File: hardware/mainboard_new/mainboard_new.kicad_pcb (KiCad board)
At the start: 2 copper layers, 59.4 x 34.5 mm, 11 parts, among them M1 LOGIC_LEVEL_CONVERTER, Q1 BS170

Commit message: #9 More rework at the pcb
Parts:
- moved 5vPower1 8.66 mm to (136.9, 97.5), turned to 180 degrees
- moved MOTOR_DRV1 3.36 mm to (144.3, 85.3)
- moved Motor_OUT1 2.86 mm to (136.7, 85.9)
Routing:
- net +5V: track 55.0 -> 44.1 mm
- net Net-(MOTOR_DRV1-Pad3): track 5.78 -> 4.55 mm
- net +3V3: track 33.0 -> 31.8 mm
- net Net-(100K1-Pad1): track 52.9 -> 52.1 mm
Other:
- board size 59.4 x 34.5 mm -> 59.4 x 32 mm

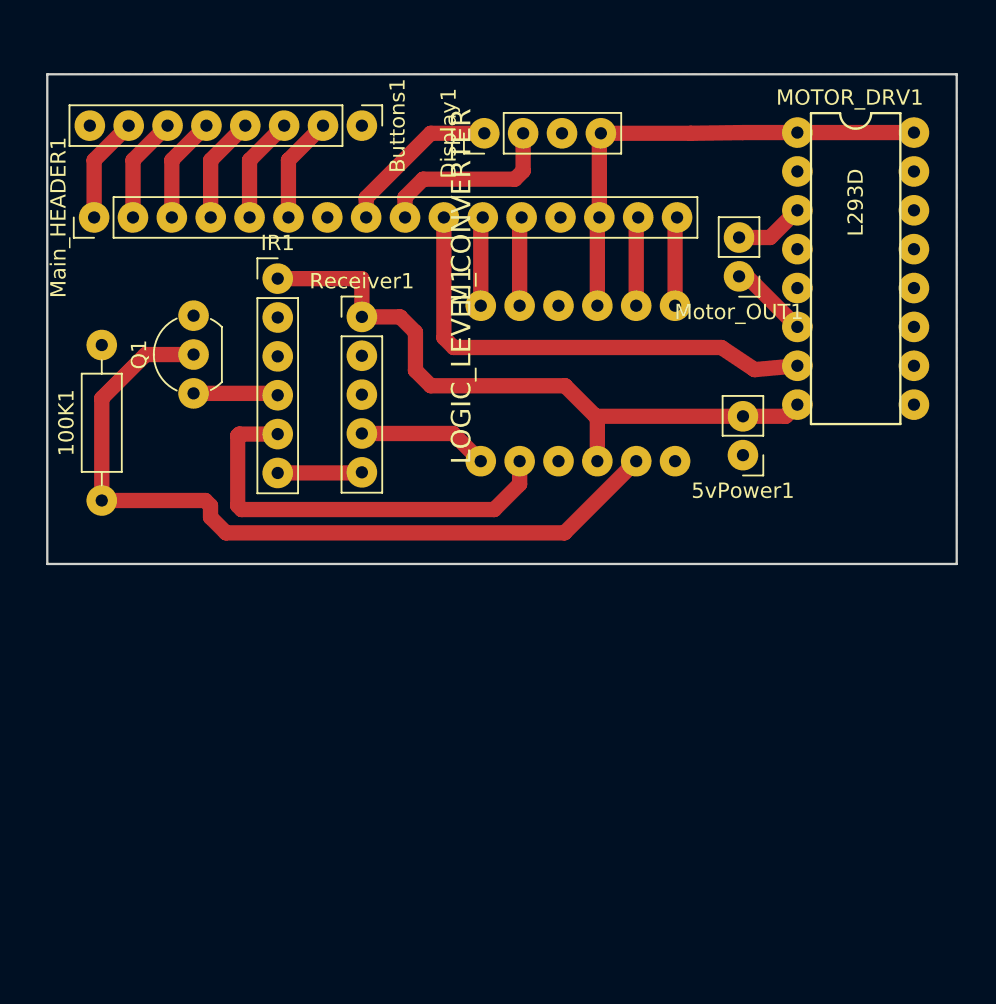
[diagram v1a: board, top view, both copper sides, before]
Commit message: #9 JST Pins added
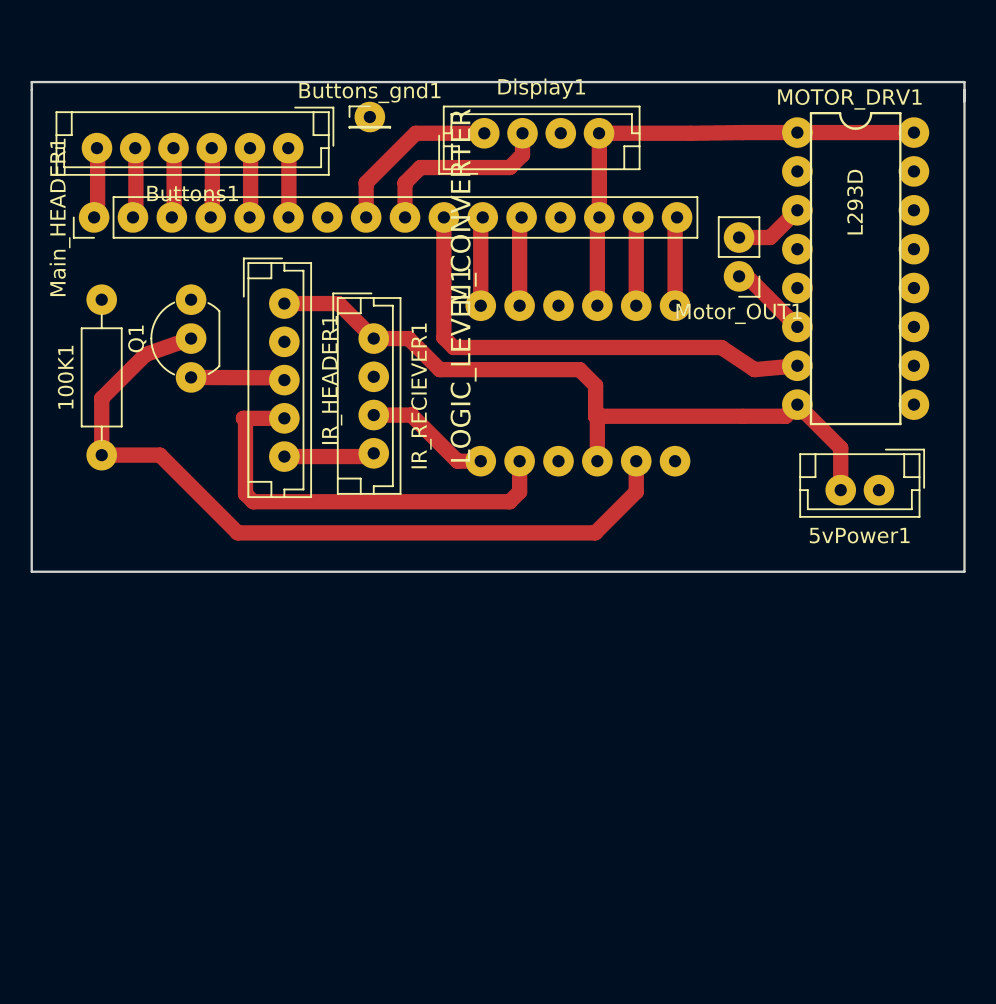
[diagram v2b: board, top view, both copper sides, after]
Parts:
- removed IR1: CONN_01X06, Socket_Strips:Socket_Strip_Straight_1x06_Pitch2.54mm
- removed Receiver1: CONN_01X05, Socket_Strips:Socket_Strip_Straight_1x05_Pitch2.54mm
- added Buttons_gnd1: CONN_01X01, Socket_Strips:Socket_Strip_Straight_1x01_Pitch1.27mm, F.Cu at (112.5, 75.4)
- added IR_HEADER1: CONN_01X05, Connectors_JST:JST_EH_B05B-EH-A_05x2.50mm_Straight, F.Cu at (106.9, 87.6)
- added IR_RECIEVER1: CONN_01X04, Connectors_JST:JST_EH_B04B-EH-A_04x2.50mm_Straight, F.Cu at (112.8, 89.9)
- 5vPower1: footprint Socket_Strips:Socket_Strip_Straight_1x02_Pitch2.54mm -> Connectors_JST:JST_EH_B02B-EH-A_02x2.50mm_Straight
- Buttons1: value CONN_01X08 -> CONN_01X06; footprint Socket_Strips:Socket_Strip_Straight_1x08_Pitch2.54mm -> Connectors_JST:JST_EH_B06B-EH-A_06x2.50mm_Straight
- Display1: footprint Socket_Strips:Socket_Strip_Straight_1x04_Pitch2.54mm -> Connectors_JST:JST_EH_B04B-EH-A_04x2.50mm_Straight
- moved 5vPower1 9.18 mm to (145.8, 99.8)
- moved Buttons1 5.03 mm to (107.2, 77.5), turned to 180 degrees
- moved 100K1 2.96 mm to (95.0, 97.5)
- moved Q1 1.06 mm to (100.8, 92.5)
- turned Display1 to 0 degrees
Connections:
- Buttons1 pad 1: GND -> Net-(Buttons1-Pad1)
- Main_HEADER1 pad 1: Net-(Buttons1-Pad7) -> Net-(Buttons1-Pad6)
- Main_HEADER1 pad 2: Net-(Buttons1-Pad6) -> Net-(Buttons1-Pad5)
- Main_HEADER1 pad 3: Net-(Buttons1-Pad5) -> Net-(Buttons1-Pad4)
- Main_HEADER1 pad 4: Net-(Buttons1-Pad4) -> Net-(Buttons1-Pad3)
- Main_HEADER1 pad 5: Net-(Buttons1-Pad3) -> Net-(Buttons1-Pad2)
- Main_HEADER1 pad 6: Net-(Buttons1-Pad2) -> Net-(Buttons1-Pad1)
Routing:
- net Net-(Buttons1-Pad7): track 6.94 -> 0.00 mm
- net Net-(Buttons1-Pad1): track 0.00 -> 4.54 mm
- net +5V: track 44.1 -> 47.8 mm
- net Net-(Buttons1-Pad2): track 6.94 -> 4.56 mm
- net Net-(Buttons1-Pad3): track 6.94 -> 4.57 mm
- net Net-(Buttons1-Pad4): track 6.94 -> 4.59 mm
- net Net-(Buttons1-Pad5): track 6.94 -> 4.61 mm
- net Net-(Buttons1-Pad6): track 6.94 -> 4.62 mm
- net Net-(100K1-Pad1): track 52.1 -> 51.1 mm
- net Net-(Display1-Pad1): track 10.7 -> 11.3 mm
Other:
- board size 59.4 x 32 mm -> 61 x 32 mm

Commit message: Flipped the mainbaord
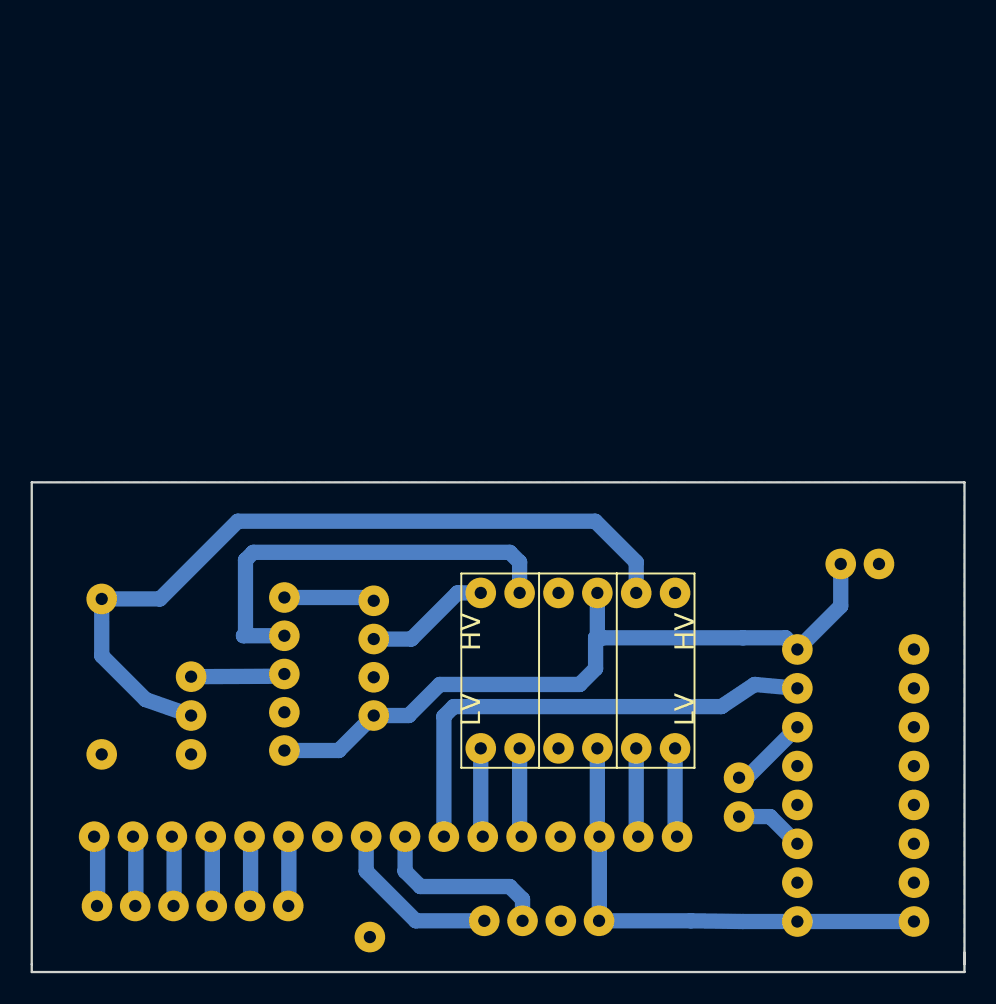
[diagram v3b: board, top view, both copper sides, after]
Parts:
- 100K1, 5vPower1, Buttons1, Buttons_gnd1, Display1, IR_HEADER1, IR_RECIEVER1, M1, MOTOR_DRV1, Main_HEADER1, Motor_OUT1, Q1: moved to B.Cu
- moved Buttons_gnd1 53.6 mm to (112.5, 129.0)
- moved Display1 51.5 mm to (120.0, 128.0)
- moved Buttons1 49.5 mm to (107.2, 127.0)
- moved Main_HEADER1 40.5 mm to (94.5, 122.5), turned to 270 degrees
- moved MOTOR_DRV1 33.8 mm to (144.3, 119.1), turned to 90 degrees
- moved Motor_OUT1 32.8 mm to (136.7, 118.6)
- moved M1 31.5 mm to (118.5, 118.0), turned to 90 degrees
- moved IR_HEADER1 29.2 mm to (106.9, 116.8), turned to 90 degrees
- moved IR_RECIEVER1 24.6 mm to (112.8, 114.6), turned to 90 degrees
- moved Q1 19.6 mm to (100.8, 112.0), turned to 270 degrees
- moved 100K1 9.40 mm to (95.0, 106.9), turned to 270 degrees
- moved 5vPower1 4.83 mm to (145.8, 104.6)
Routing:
- added copper zone on B.Cu, net GND
- removed copper zone on F.Cu, net GND
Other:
- outline, holes or cut-outs redrawn
